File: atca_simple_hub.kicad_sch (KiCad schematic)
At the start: 1 part

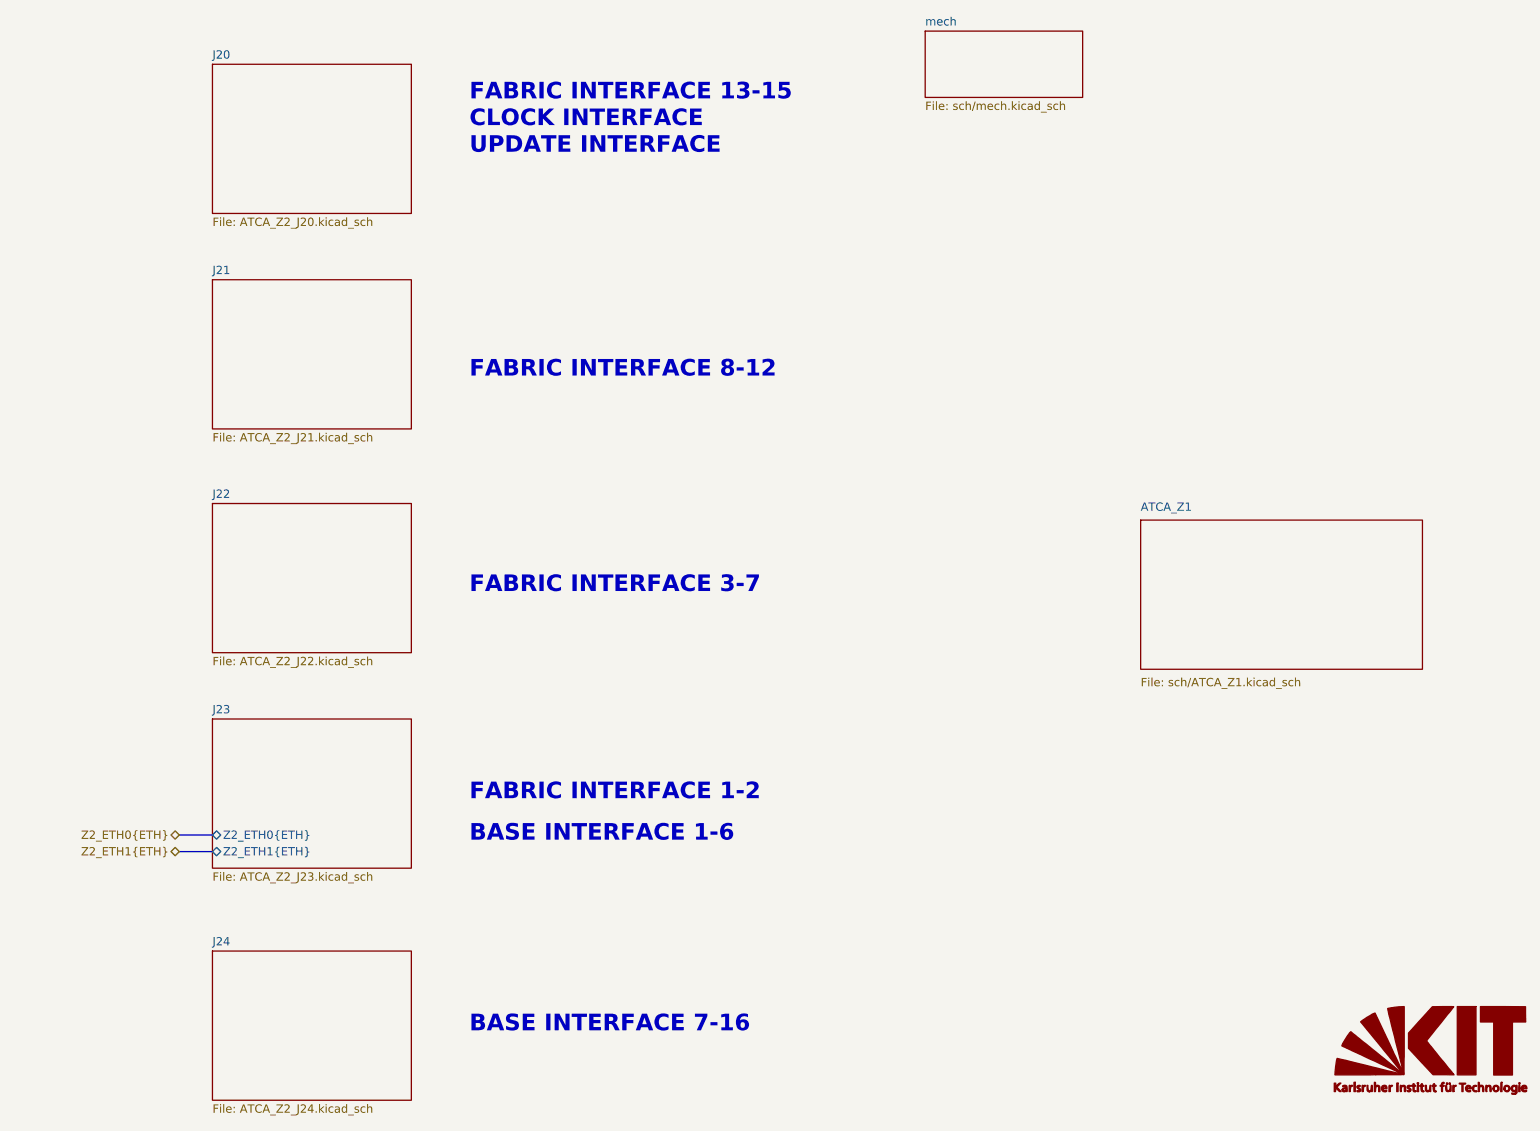
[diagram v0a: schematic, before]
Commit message: added magjacks
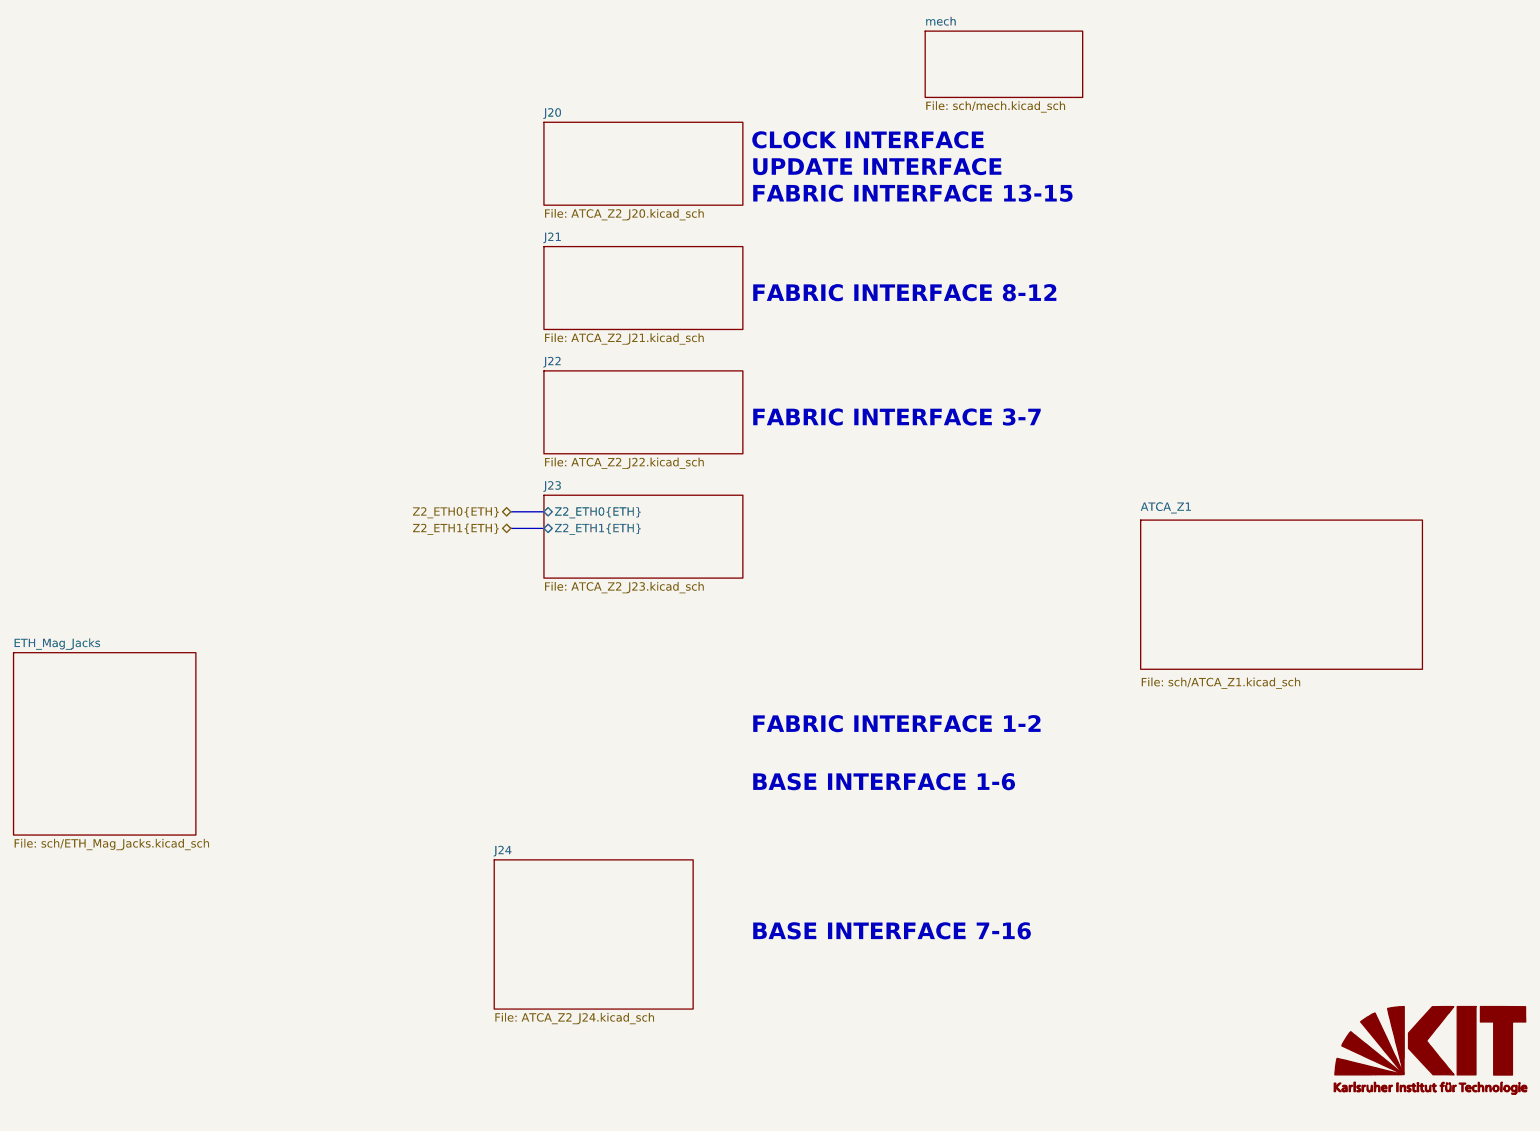
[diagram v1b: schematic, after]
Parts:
- G1: footprint KIT_Graphic:KIT_LOGO -> project:KIT_LOGO
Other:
- added sheet ETH_Mag_Jacks (sch/ETH_Mag_Jacks.kicad_sch)
- note added: "CLOCK INTERFACE UPDATE INTERFACE FABRIC INTERFACE 13-15"
- note removed: "FABRIC INTERFACE 13-15 CLOCK INTERFACE UPDATE INTERFACE"
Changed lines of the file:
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@@
     (comment 4 "Licensed under CERN-OHL-S-2.0")
   )
-  (bus (pts (xy 76.2 143.51) (xy 81.28 143.51))
+  (bus (pts (xy 127 93.98) (xy 132.08 93.98))
     (stroke (width 0) (type default))
   )
-  (bus (pts (xy 76.2 140.97) (xy 81.28 140.97))
+  (bus (pts (xy 127 91.44) (xy 132.08 91.44))
     (stroke (width 0) (type default))
   )
-  (text "BASE INTERFACE 1-6" (at 120.65 142.24 0)
+  (text "BASE INTERFACE 1-6" (at 163.83 134.62 0)
     (effects (font (size 2.54 2.54) (thickness 0.508) bold) (justify left bottom))
   )
-  (text "FABRIC INTERFACE 13-15\nCLOCK INTERFACE\nUPDATE INTERFACE"
-    (at 120.65 36.83 0)
+  (text "CLOCK INTERFACE\nUPDATE INTERFACE\nFABRIC INTERFACE 13-15"
+    (at 163.83 44.45 0)
     (effects (font (size 2.54 2.54) (thickness 0.508) bold) (justify left bottom))
   )
-  (text "BASE INTERFACE 7-16" (at 120.65 171.45 0)
+  (text "BASE INTERFACE 7-16" (at 163.83 157.48 0)
     (effects (font (size 2.54 2.54) (thickness 0.508) bold) (justify left bottom))
   )
-  (text "FABRIC INTERFACE 8-12" (at 120.65 71.12 0)
+  (text "FABRIC INTERFACE 8-12" (at 163.83 59.69 0)
     (effects (font (size 2.54 2.54) (thickness 0.508) bold) (justify left bottom))
   )
-  (text "FABRIC INTERFACE 3-7" (at 120.65 104.14 0)
+  (text "FABRIC INTERFACE 3-7" (at 163.83 78.74 0)
     (effects (font (size 2.54 2.54) (thickness 0.508) bold) (justify left bottom))
   )
-  (text "FABRIC INTERFACE 1-2" (at 120.65 135.89 0)
+  (text "FABRIC INTERFACE 1-2" (at 163.83 125.73 0)
     (effects (font (size 2.54 2.54) (thickness 0.508) bold) (justify left bottom))
   )
-  (hierarchical_label "Z2_ETH1{ETH}" (shape bidirectional) (at 76.2 143.51 180) (fields_autoplaced)
+  (hierarchical_label "Z2_ETH1{ETH}" (shape bidirectional) (at 127 93.98 180) (fields_autoplaced)
     (effects (font (size 1.27 1.27)) (justify right))
   )
-  (hierarchical_label "Z2_ETH0{ETH}" (shape bidirectional) (at 76.2 140.97 180) (fields_autoplaced)
+  (hierarchical_label "Z2_ETH0{ETH}" (shape bidirectional) (at 127 91.44 180) (fields_autoplaced)
     (effects (font (size 1.27 1.27)) (justify right))
   )
@@
       (effects (font (size 1.524 1.524)) hide)
     )
-    (property "Footprint" "KIT_Graphic:KIT_LOGO" (at 267.97 173.99 0)
+    (property "Footprint" "project:KIT_LOGO" (at 267.97 173.99 0)
       (effects (font (size 3.9878 3.9878)) hide)
     )
@@
     )
   )
-  (sheet (at 81.28 123.19) (size 30.48 22.86) (fields_autoplaced)
+  (sheet (at 132.08 88.9) (size 30.48 12.7) (fields_autoplaced)
     (stroke (width 0.1524) (type solid))
     (fill (color 0 0 0 0.0000))
-    (property "Sheetname" "J23" (at 81.28 122.4784 0)
+    (property "Sheetname" "J23" (at 132.08 88.1884 0)
       (effects (font (size 1.27 1.27)) (justify left bottom))
     )
-    (property "Sheetfile" "ATCA_Z2_J23.kicad_sch" (at 81.28 146.6346 0)
+    (property "Sheetfile" "ATCA_Z2_J23.kicad_sch" (at 132.08 102.1846 0)
       (effects (font (size 1.27 1.27)) (justify left top))
     )
-    (pin "Z2_ETH0{ETH}" bidirectional (at 81.28 140.97 180)
+    (pin "Z2_ETH0{ETH}" bidirectional (at 132.08 91.44 180)
       (effects (font (size 1.27 1.27)) (justify left))
     )
-    (pin "Z2_ETH1{ETH}" bidirectional (at 81.28 143.51 180)
+    (pin "Z2_ETH1{ETH}" bidirectional (at 132.08 93.98 180)
       (effects (font (size 1.27 1.27)) (justify left))
     )
@@
     )
   )
-  (sheet (at 81.28 158.75) (size 30.48 22.86) (fields_autoplaced)
+  (sheet (at 50.8 113.03) (size 27.94 27.94) (fields_autoplaced)
     (stroke (width 0.1524) (type solid))
     (fill (color 0 0 0 0.0000))
-    (property "Sheetname" "J24" (at 81.28 158.0384 0)
+    (property "Sheetname" "ETH_Mag_Jacks" (at 50.8 112.3184 0)
       (effects (font (size 1.27 1.27)) (justify left bottom))
     )
-    (property "Sheetfile" "ATCA_Z2_J24.kicad_sch" (at 81.28 182.1946 0)
+    (property "Sheetfile" "sch/ETH_Mag_Jacks.kicad_sch" (at 50.8 141.5546 0)
+      (effects (font (size 1.27 1.27)) (justify left top))
+    )
+    (instances
+      (project "atca_simple_hub"
+        (path "/b1bf14e0-f6d2-45a7-b67f-6500a354b7ad" (page "9"))
+      )
+    )
+  )
+  (sheet (at 124.46 144.78) (size 30.48 22.86) (fields_autoplaced)
+    (stroke (width 0.1524) (type solid))
+    (fill (color 0 0 0 0.0000))
+    (property "Sheetname" "J24" (at 124.46 144.0684 0)
+      (effects (font (size 1.27 1.27)) (justify left bottom))
+    )
+    (property "Sheetfile" "ATCA_Z2_J24.kicad_sch" (at 124.46 168.2246 0)
       (effects (font (size 1.27 1.27)) (justify left top))
     )
@@
     )
   )
-  (sheet (at 81.28 90.17) (size 30.48 22.86) (fields_autoplaced)
+  (sheet (at 132.08 69.85) (size 30.48 12.7) (fields_autoplaced)
     (stroke (width 0.1524) (type solid))
     (fill (color 0 0 0 0.0000))
-    (property "Sheetname" "J22" (at 81.28 89.4584 0)
+    (property "Sheetname" "J22" (at 132.08 69.1384 0)
       (effects (font (size 1.27 1.27)) (justify left bottom))
     )
-    (property "Sheetfile" "ATCA_Z2_J22.kicad_sch" (at 81.28 113.6146 0)
+    (property "Sheetfile" "ATCA_Z2_J22.kicad_sch" (at 132.08 83.1346 0)
       (effects (font (size 1.27 1.27)) (justify left top))
     )
@@
     )
   )
-  (sheet (at 81.28 55.88) (size 30.48 22.86) (fields_autoplaced)
+  (sheet (at 132.08 50.8) (size 30.48 12.7) (fields_autoplaced)
     (stroke (width 0.1524) (type solid))
     (fill (color 0 0 0 0.0000))
-    (property "Sheetname" "J21" (at 81.28 55.1684 0)
+    (property "Sheetname" "J21" (at 132.08 50.0884 0)
       (effects (font (size 1.27 1.27)) (justify left bottom))
     )
-    (property "Sheetfile" "ATCA_Z2_J21.kicad_sch" (at 81.28 79.3246 0)
+    (property "Sheetfile" "ATCA_Z2_J21.kicad_sch" (at 132.08 64.0846 0)
       (effects (font (size 1.27 1.27)) (justify left top))
     )
@@
     )
   )
-  (sheet (at 81.28 22.86) (size 30.48 22.86) (fields_autoplaced)
+  (sheet (at 132.08 31.75) (size 30.48 12.7) (fields_autoplaced)
     (stroke (width 0.1524) (type solid))
     (fill (color 0 0 0 0.0000))
-    (property "Sheetname" "J20" (at 81.28 22.1484 0)
+    (property "Sheetname" "J20" (at 132.08 31.0384 0)
       (effects (font (size 1.27 1.27)) (justify left bottom))
     )
-    (property "Sheetfile" "ATCA_Z2_J20.kicad_sch" (at 81.28 46.3046 0)
+    (property "Sheetfile" "ATCA_Z2_J20.kicad_sch" (at 132.08 45.0346 0)
       (effects (font (size 1.27 1.27)) (justify left top))
     )
